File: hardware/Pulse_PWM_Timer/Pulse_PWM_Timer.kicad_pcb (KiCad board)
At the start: 4 copper layers, 27.9 x 43.2 mm, 57 parts, among them J1 Action Input, J2 Action Output, J3 Load, Q1 MMBT5551L, Q2 SI2301CDS-T1-GE3, U1 NE555PWR, U2 LM393QT, U3 DRV8876PWPR

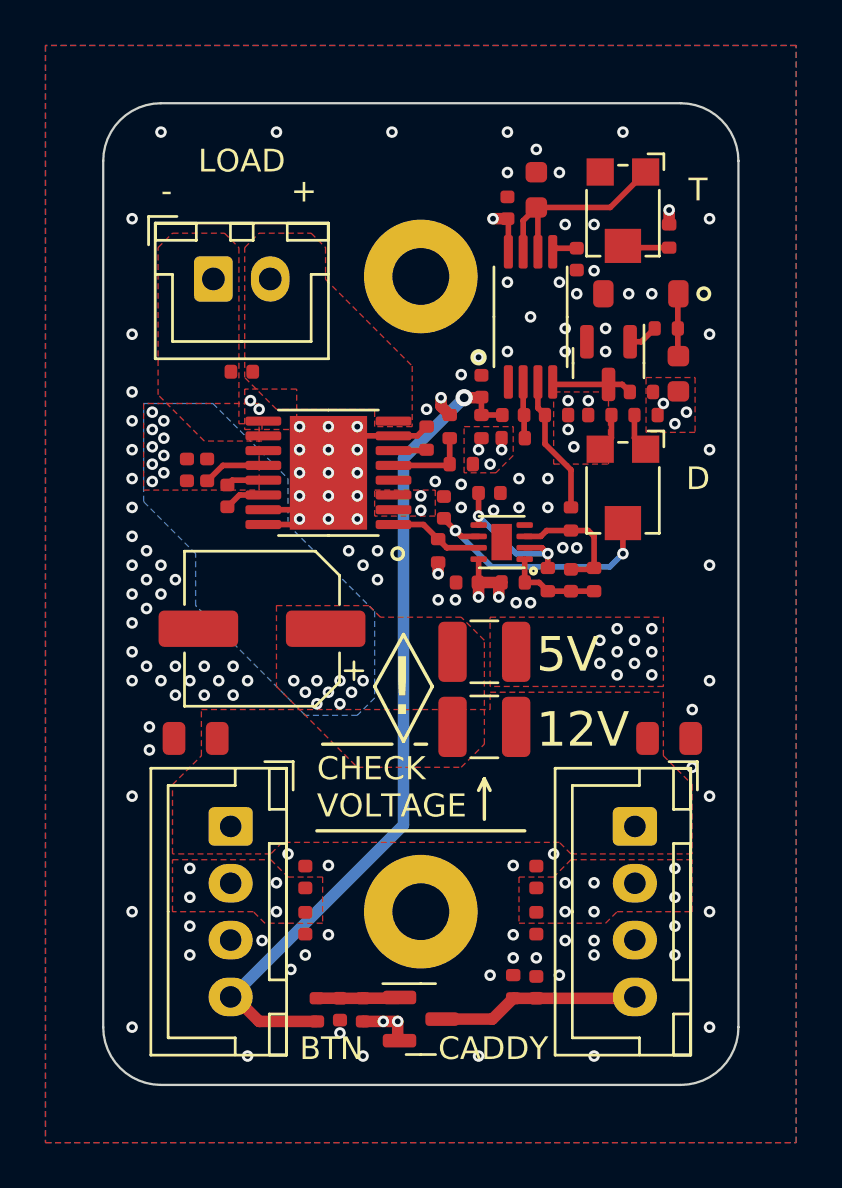
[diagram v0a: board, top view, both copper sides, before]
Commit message: On-delay applied to motor controller
555 on-delay tied to DRV8876 sleep line. Increased track widths to components with large thermal reliefs to mitigate tombstoning.
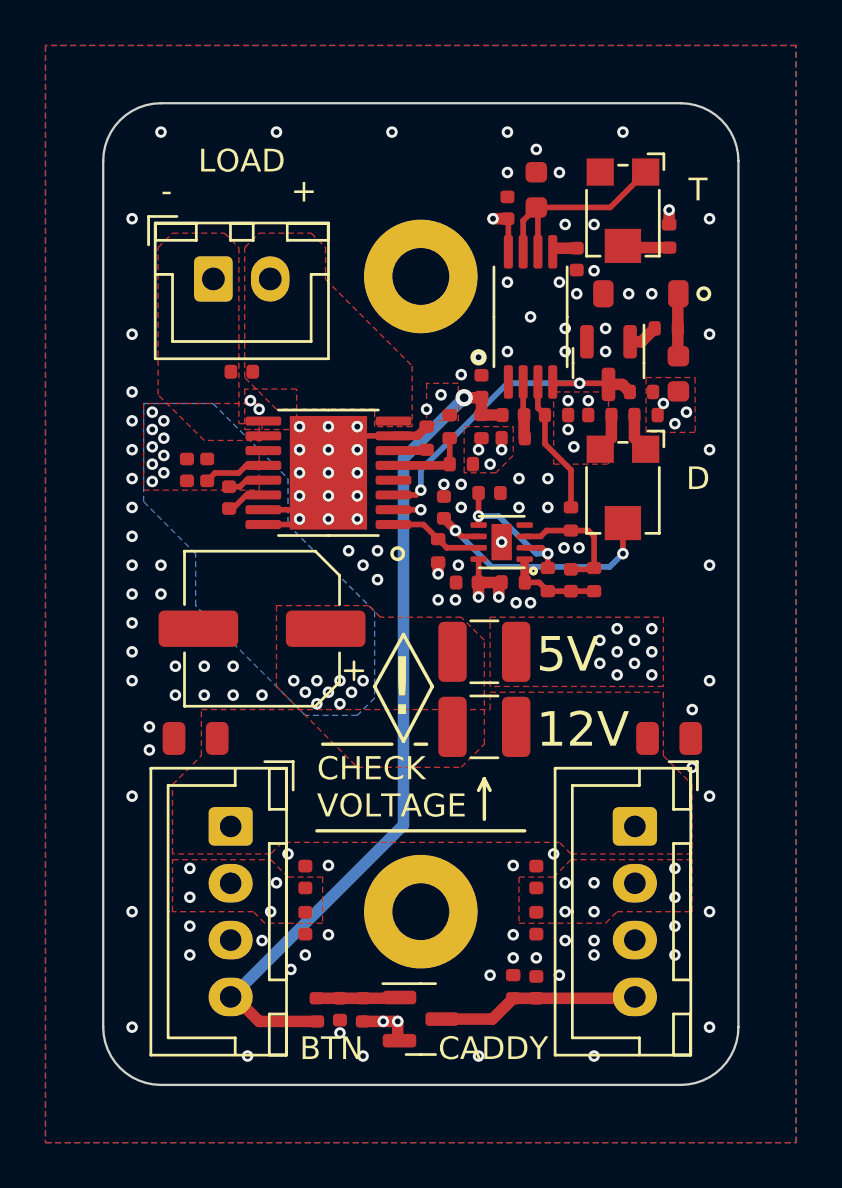
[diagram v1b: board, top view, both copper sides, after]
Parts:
- moved C20 0.11 mm to (132.5, 101.2)
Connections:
- U2 pad 9: (no net) -> GND
- U3 pad 3: +5V -> ON_DELAY
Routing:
- net ON_DELAY: track 3.57 -> 14.3 mm, vias 0 -> 2
- net +5V: track 9.07 -> 10.3 mm, vias 35 -> 34
- net GND: track 7.36 -> 6.44 mm, vias 135 -> 128
